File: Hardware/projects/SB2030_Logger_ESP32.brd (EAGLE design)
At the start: 96.8 x 48.4 mm, 105 parts, among them T2 S8050, T3 S8050, T4 S8050, U1 ESP32-WROOM-32E, U2 TJA1051T/3, U3 LSM6DS3TR-C, U4 AMS1117-3.3, U5 SN65C1168NSR

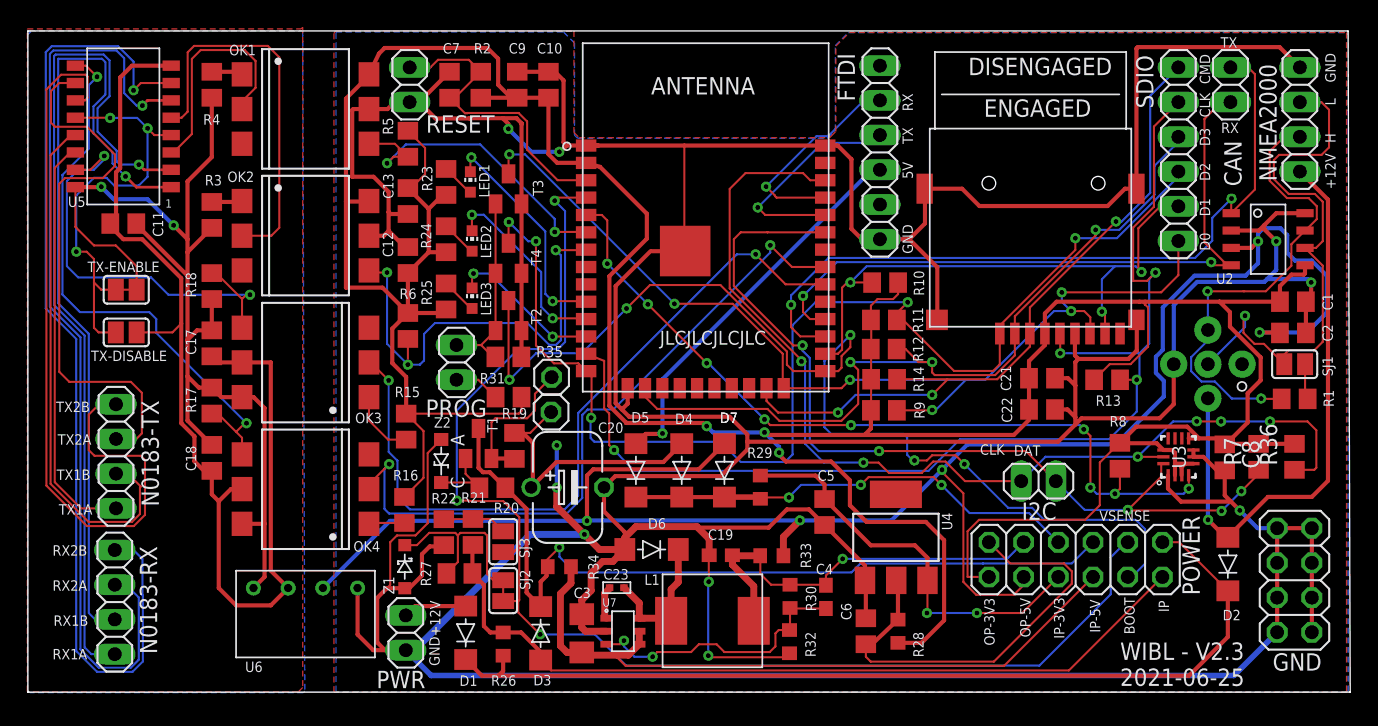
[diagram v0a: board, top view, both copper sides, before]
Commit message: Fixed labelling on schematic for INT1 from IMU, and cleaned up some notation; fixed routing and airwires on board so that DRC passes.
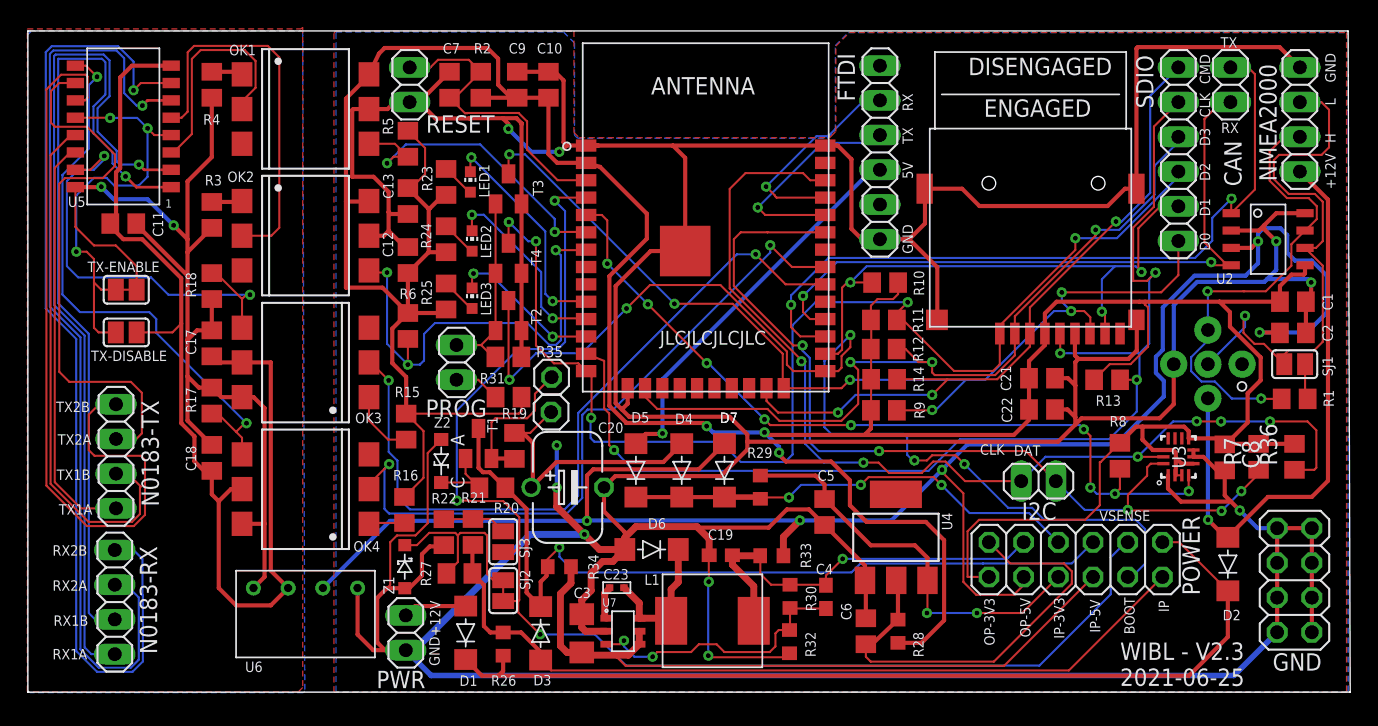
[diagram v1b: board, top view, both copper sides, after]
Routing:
- net GND: track 488.6 -> 490.5 mm
- net +3V3: track 286.6 -> 285.0 mm
